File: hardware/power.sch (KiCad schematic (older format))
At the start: 16 parts, among them CON1 VEXT, P6 VEXT, U6 LD3985M33R

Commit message: LTC4417 for automatic power source switching
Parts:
- removed D1: FSV1045V, rgb-matrix:DIODE-TO-277A, symbol D_Schottky_Small
- removed D2: CDBA340L, Diodes_SMD:SMA_Standard, symbol D_Schottky_Small
- added C19, C20: 10uF, Capacitors_SMD:C_0805, symbol C
- added Q1, Q2: IRF7324PBF, SO-8, symbol IRF7324PBF
- added R31, R32: 1M, symbol R
- added R33, R36: 412k, symbol R
- added R34: 33.2k, symbol R
- added R35: 100k, symbol R
- added R37: 37.4k, symbol R
- added R38: 95.3k, symbol R
- added U8: LTC4417, symbol LTC4417
- added U9: 74x2G04, symbol 74x2G04
- D1: renamed from 3V1; Comment (none) -> 3.3V
- D2: renamed from Vext1; Comment (none) -> VEXT
- D3: renamed from Vbus1; Comment (none) -> VBUS
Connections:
- net labels added: VCC
- wire segments 36 -> 109
- no-connect marks 0 -> 4
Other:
- moved on the sheet: C12, C13, C14, C15, C9, CON1, D1, D2, D3, P6, R28, R29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

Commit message: Assign footprints
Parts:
- Q1, Q2: footprint SO-8 -> Power_Integrations:SO-8
- R31, R32, R33, R34, R35, R36, R37, R38: footprint (none) -> Resistors_SMD:R_0805
- U8: footprint (none) -> Housings_SSOP:SSOP-24_3.9x8.7mm_Pitch0.635mm
- U9: footprint (none) -> TO_SOT_Packages_SMD:SOT-23-6
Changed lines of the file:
@@
 F 0 "U8" H 4300 5000 60  0000 C CNN
 F 1 "LTC4417" H 4300 5200 60  0000 C CNN
-F 2 "" H 4300 5100 60  0001 C CNN
+F 2 "Housings_SSOP:SSOP-24_3.9x8.7mm_Pitch0.635mm" H 4300 5100 60  0001 C CNN
 F 3 "" H 4300 5100 60  0001 C CNN
 	1    4300 5100
@@
 F 0 "R31" V 6080 4000 50  0000 C CNN
 F 1 "1M" V 6000 4000 50  0000 C CNN
-F 2 "" V 5930 4000 50  0000 C CNN
+F 2 "Resistors_SMD:R_0805" V 5930 4000 50  0001 C CNN
 F 3 "" H 6000 4000 50  0000 C CNN
 	1    6000 4000
@@
 F 0 "R32" V 6230 4000 50  0000 C CNN
 F 1 "1M" V 6150 4000 50  0000 C CNN
-F 2 "" V 6080 4000 50  0000 C CNN
+F 2 "Resistors_SMD:R_0805" V 6080 4000 50  0001 C CNN
 F 3 "" H 6150 4000 50  0000 C CNN
 	1    6150 4000
@@
 F 0 "Q1" V 3350 2100 50  0000 L CNN
 F 1 "IRF7324PBF" V 3450 1700 50  0000 L CNN
-F 2 "SO-8" H 3350 2075 50  0001 L CNN
+F 2 "Power_Integrations:SO-8" H 3350 2075 50  0001 L CNN
 F 3 "" H 2400 2550 50  0000 L CNN
 	1    3100 2150
@@
 F 0 "Q1" V 3850 2100 50  0000 L CNN
 F 1 "IRF7324PBF" H 3850 2150 50  0001 L CNN
-F 2 "SO-8" H 3850 2075 50  0001 L CNN
+F 2 "Power_Integrations:SO-8" H 3850 2075 50  0001 L CNN
 F 3 "" H 2900 2550 50  0000 L CNN
 	2    3600 2150
@@
 F 0 "Q2" V 4250 2800 50  0000 L CNN
 F 1 "IRF7324PBF" V 4350 2400 50  0000 L CNN
-F 2 "SO-8" H 4250 2775 50  0001 L CNN
+F 2 "Power_Integrations:SO-8" H 4250 2775 50  0001 L CNN
 F 3 "" H 3300 3250 50  0000 L CNN
 	1    4000 2850
@@
 F 0 "Q2" V 4750 2800 50  0000 L CNN
 F 1 "IRF7324PBF" H 4750 2850 50  0001 L CNN
-F 2 "SO-8" H 4750 2775 50  0001 L CNN
+F 2 "Power_Integrations:SO-8" H 4750 2775 50  0001 L CNN
 F 3 "" H 3800 3250 50  0000 L CNN
 	2    4500 2850
@@
 F 0 "R36" V 2880 3950 50  0000 C CNN
 F 1 "412k" V 2800 3950 50  0000 C CNN
-F 2 "" V 2730 3950 50  0000 C CNN
+F 2 "Resistors_SMD:R_0805" V 2730 3950 50  0001 C CNN
 F 3 "" H 2800 3950 50  0000 C CNN
 	1    2800 3950
@@
 F 0 "R37" V 2880 4250 50  0000 C CNN
 F 1 "37.4k" V 2800 4250 50  0000 C CNN
-F 2 "" V 2730 4250 50  0000 C CNN
+F 2 "Resistors_SMD:R_0805" V 2730 4250 50  0001 C CNN
 F 3 "" H 2800 4250 50  0000 C CNN
 	1    2800 4250
@@
 F 0 "R33" V 2780 5050 50  0000 C CNN
 F 1 "412k" V 2700 5050 50  0000 C CNN
-F 2 "" V 2630 5050 50  0000 C CNN
+F 2 "Resistors_SMD:R_0805" V 2630 5050 50  0001 C CNN
 F 3 "" H 2700 5050 50  0000 C CNN
 	1    2700 5050
@@
 F 0 "R34" V 2780 5350 50  0000 C CNN
 F 1 "33.2k" V 2700 5350 50  0000 C CNN
-F 2 "" V 2630 5350 50  0000 C CNN
+F 2 "Resistors_SMD:R_0805" V 2630 5350 50  0001 C CNN
 F 3 "" H 2700 5350 50  0000 C CNN
 	1    2700 5350
@@
 F 0 "R38" V 2880 4550 50  0000 C CNN
 F 1 "95.3k" V 2800 4550 50  0000 C CNN
-F 2 "" V 2730 4550 50  0000 C CNN
+F 2 "Resistors_SMD:R_0805" V 2730 4550 50  0001 C CNN
 F 3 "" H 2800 4550 50  0000 C CNN
 	1    2800 4550
@@
 F 0 "R35" V 2780 5650 50  0000 C CNN
 F 1 "100k" V 2700 5650 50  0000 C CNN
-F 2 "" V 2630 5650 50  0000 C CNN
+F 2 "Resistors_SMD:R_0805" V 2630 5650 50  0001 C CNN
 F 3 "" H 2700 5650 50  0000 C CNN
 	1    2700 5650
@@
 F 0 "U9" H 6895 4315 50  0000 C CNN
 F 1 "74x2G04" H 6890 4075 50  0000 C CNN
-F 2 "" H 6700 4200 50  0000 C CNN
+F 2 "TO_SOT_Packages_SMD:SOT-23-6" H 6700 4200 50  0001 C CNN
 F 3 "" H 6700 4200 50  0000 C CNN
 	1    6700 4200
@@
 F 0 "U9" H 6895 4815 50  0000 C CNN
 F 1 "74x2G04" H 6890 4575 50  0000 C CNN
-F 2 "" H 6700 4700 50  0000 C CNN
+F 2 "TO_SOT_Packages_SMD:SOT-23-6" H 6700 4700 50  0001 C CNN
 F 3 "" H 6700 4700 50  0000 C CNN
 	2    6700 4700
@@
 	3450 3350 3450 2350
 Wire Wire Line
-	3150 2350 3450 2350
-Wire Wire Line
-	3450 2350 3550 2350
+	3150 2350 3550 2350
 Wire Wire Line
 	3350 2050 3350 3350
@@
 	5250 3300 5250 3350
 Wire Wire Line
-	4900 3300 5150 3300
-Wire Wire Line
-	5150 3300 5250 3300
+	4900 3300 5250 3300
 Wire Wire Line
 	5150 3350 5150 3300
@@
 	2850 6600 2900 6600
 Wire Wire Line
-	2850 6000 2850 6300
-Wire Wire Line
-	2850 6300 2850 6600
-Wire Wire Line
-	2850 6600 2850 6650
-Wire Wire Line
-	6150 4150 6150 4300
-Wire Wire Line
-	6150 4300 6150 4700
+	2850 6000 2850 6650
+Wire Wire Line
+	6150 4150 6150 4700
 Wire Wire Line
 	5700 4300 6150 4300
@@
 	6000 4200 6000 4150
 Wire Wire Line
-	5700 4200 6000 4200
-Wire Wire Line
-	6000 4200 6250 4200
-Wire Wire Line
-	6000 3750 6000 3800
-Wire Wire Line
-	6000 3800 6000 3850
+	5700 4200 6250 4200
+Wire Wire Line
+	6000 3750 6000 3850
 Wire Wire Line
 	6150 3800 6000 3800
@@
 	5700 6350 5800 6350
 Wire Wire Line
-	1200 2650 2150 2650
-Wire Wire Line
-	2150 2650 2700 2650
-Wire Wire Line
-	2700 2650 3800 2650
+	1200 2650 3800 2650
 Wire Wire Line
 	9550 1500 9550 1600
@@
 	1550 1400 1200 1400
 Wire Wire Line
-	1550 1950 1650 1950
-Wire Wire Line
-	1650 1950 2150 1950
-Wire Wire Line
-	2150 1950 2800 1950
-Wire Wire Line
-	2800 1950 2900 1950
+	1550 1950 2900 1950
 Connection ~ 1550 2150
 Wire Wire Line
-	1550 2050 1550 2150
-Wire Wire Line
-	1550 2150 1550 2250
+	1550 2050 1550 2250
 Connection ~ 8700 1600
 Wire Wire Line
@@
 Connection ~ 7050 2150
 Wire Wire Line
-	7050 2150 7250 2150
-Wire Wire Line
-	7250 2150 7800 2150
-Wire Wire Line
-	7800 2150 8250 2150
-Wire Wire Line
-	8250 2150 8450 2150
-Wire Wire Line
-	8450 2150 8700 2150
+	7050 2150 8700 2150
 Connection ~ 7250 1750
 Connection ~ 7050 1600
 Connection ~ 7250 1600
 Wire Wire Line
-	7250 1600 7250 1750
-Wire Wire Line
-	7250 1750 7250 1850
+	7250 1600 7250 1850
 Wire Wire Line
 	7350 1750 7250 1750
 Wire Wire Line
-	8250 1600 8450 1600
-Wire Wire Line
-	8450 1600 8700 1600
-Wire Wire Line
-	7050 1600 7250 1600
-Wire Wire Line
-	7250 1600 7350 1600
-Wire Wire Line
-	7050 1550 7050 1600
-Wire Wire Line
-	7050 1600 7050 1700
-Wire Wire Line
-	8700 1450 8700 1600
-Wire Wire Line
-	8700 1600 8700 1850
+	8250 1600 8700 1600
+Wire Wire Line
+	7050 1600 7350 1600
+Wire Wire Line
+	7050 1550 7050 1700
+Wire Wire Line
+	8700 1450 8700 1850
 Wire Wire Line
 	8450 2150 8450 1950
 Wire Wire Line
-	7050 2000 7050 2150
-Wire Wire Line
-	7050 2150 7050 2200
+	7050 2000 7050 2200
 Wire Wire Line
 	3800 2650 3800 2750
@@
 	4450 3100 4450 3050
 Wire Wire Line
-	4050 3100 4350 3100
-Wire Wire Line
-	4350 3100 4450 3100
+	4050 3100 4450 3100
 Wire Wire Line
 	4050 3050 4050 3100
 Connection ~ 4250 2750
 Wire Wire Line
-	4200 2750 4250 2750
-Wire Wire Line
-	4250 2750 4300 2750
+	4200 2750 4300 2750
 Wire Wire Line
 	4250 2750 4250 3350
@@
 Connection ~ 3350 2050
 Wire Wire Line
-	3300 2050 3350 2050
-Wire Wire Line
-	3350 2050 3400 2050
+	3300 2050 3400 2050
 Connection ~ 5150 3300
 Wire Wire Line
-	5750 1850 5750 1950
-Wire Wire Line
-	5750 1950 5750 2650
-Wire Wire Line
-	5750 2650 5750 3800
+	5750 1850 5750 3800
 Wire Wire Line
 	4700 2650 4700 2750
@@
 Connection ~ 5750 2650
 Wire Wire Line
-	10850 1450 10850 1700
+	10850 1700 10850 1450
 Wire Wire Line
 	10600 1450 10600 1700
@@
 	10350 1450 10350 1700
 Wire Wire Line
-	10350 1700 10600 1700
-Wire Wire Line
-	10600 1700 10850 1700
+	10350 1700 10850 1700
 Connection ~ 10600 1700
 $EndSCHEMATC

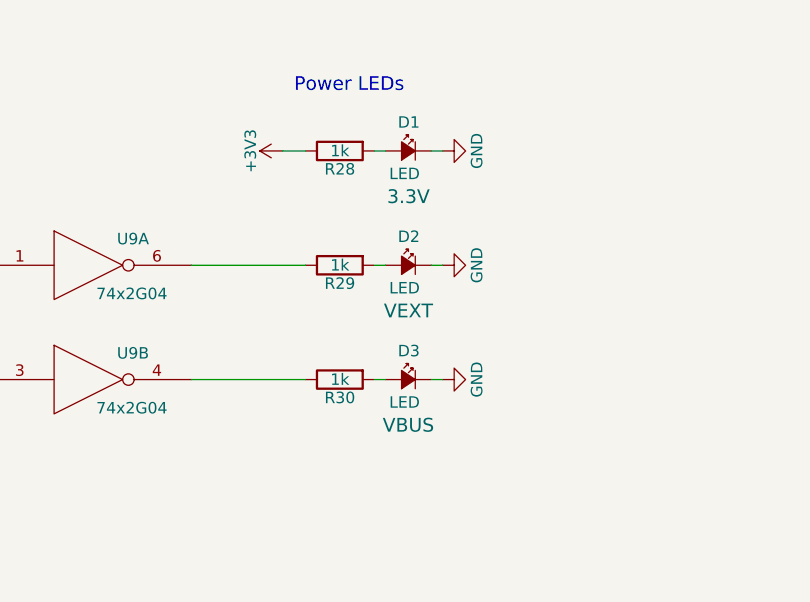
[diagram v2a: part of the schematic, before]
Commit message: Fix IRF7324 footprint
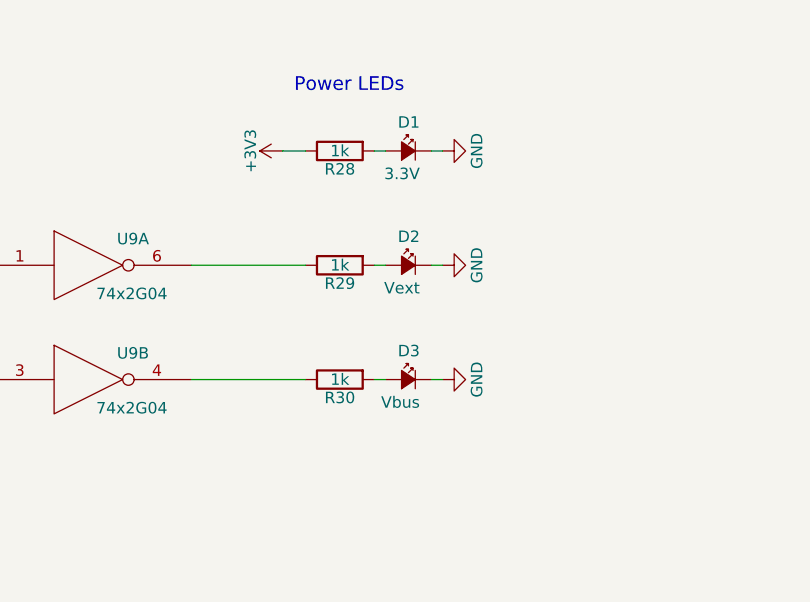
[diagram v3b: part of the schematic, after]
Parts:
- D1: value LED -> 3.3V; Comment 3.3V -> (none)
- D2: value LED -> Vext; Comment VEXT -> (none)
- D3: value LED -> Vbus; Comment VBUS -> (none)
- Q1, Q2: footprint Power_Integrations:SO-8 -> rgb-matrix:SOIC-8
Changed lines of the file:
@@
 P 8100 4200
 F 0 "D2" H 8050 4325 50  0000 L CNN
-F 1 "LED" H 8050 4100 50  0000 L CNN
+F 1 "Vext" H 8050 4100 50  0000 L CNN
 F 2 "LEDs:LED_1206" V 8100 4200 50  0001 C CNN
 F 3 "" V 8100 4200 50  0000 C CNN
-F 4 "VEXT" H 8100 4000 60  0000 C CNN "Comment"
 	1    8100 4200
 	-1   0    0    -1
@@
 P 8100 4700
 F 0 "D3" H 8050 4825 50  0000 L CNN
-F 1 "LED" H 8050 4600 50  0000 L CNN
+F 1 "Vbus" H 8050 4600 50  0000 L CNN
 F 2 "LEDs:LED_1206" V 8100 4700 50  0001 C CNN
 F 3 "" V 8100 4700 50  0000 C CNN
-F 4 "VBUS" H 8100 4500 60  0000 C CNN "Comment"
 	1    8100 4700
 	-1   0    0    -1
@@
 P 8100 3700
 F 0 "D1" H 8050 3825 50  0000 L CNN
-F 1 "LED" H 8050 3600 50  0000 L CNN
+F 1 "3.3V" H 8050 3600 50  0000 L CNN
 F 2 "LEDs:LED_1206" V 8100 3700 50  0001 C CNN
 F 3 "" V 8100 3700 50  0000 C CNN
-F 4 "3.3V" H 8100 3500 60  0000 C CNN "Comment"
 	1    8100 3700
 	-1   0    0    -1
@@
 F 0 "Q1" V 3350 2100 50  0000 L CNN
 F 1 "IRF7324PBF" V 3450 1700 50  0000 L CNN
-F 2 "Power_Integrations:SO-8" H 3350 2075 50  0001 L CNN
+F 2 "rgb-matrix:SOIC-8" H 3350 2075 50  0001 L CNN
 F 3 "" H 2400 2550 50  0000 L CNN
 	1    3100 2150
@@
 F 0 "Q1" V 3850 2100 50  0000 L CNN
 F 1 "IRF7324PBF" H 3850 2150 50  0001 L CNN
-F 2 "Power_Integrations:SO-8" H 3850 2075 50  0001 L CNN
+F 2 "rgb-matrix:SOIC-8" H 3850 2075 50  0001 L CNN
 F 3 "" H 2900 2550 50  0000 L CNN
 	2    3600 2150
@@
 F 0 "Q2" V 4250 2800 50  0000 L CNN
 F 1 "IRF7324PBF" V 4350 2400 50  0000 L CNN
-F 2 "Power_Integrations:SO-8" H 4250 2775 50  0001 L CNN
+F 2 "rgb-matrix:SOIC-8" H 4250 2775 50  0001 L CNN
 F 3 "" H 3300 3250 50  0000 L CNN
 	1    4000 2850
@@
 F 0 "Q2" V 4750 2800 50  0000 L CNN
 F 1 "IRF7324PBF" H 4750 2850 50  0001 L CNN
-F 2 "Power_Integrations:SO-8" H 4750 2775 50  0001 L CNN
+F 2 "rgb-matrix:SOIC-8" H 4750 2775 50  0001 L CNN
 F 3 "" H 3800 3250 50  0000 L CNN
 	2    4500 2850

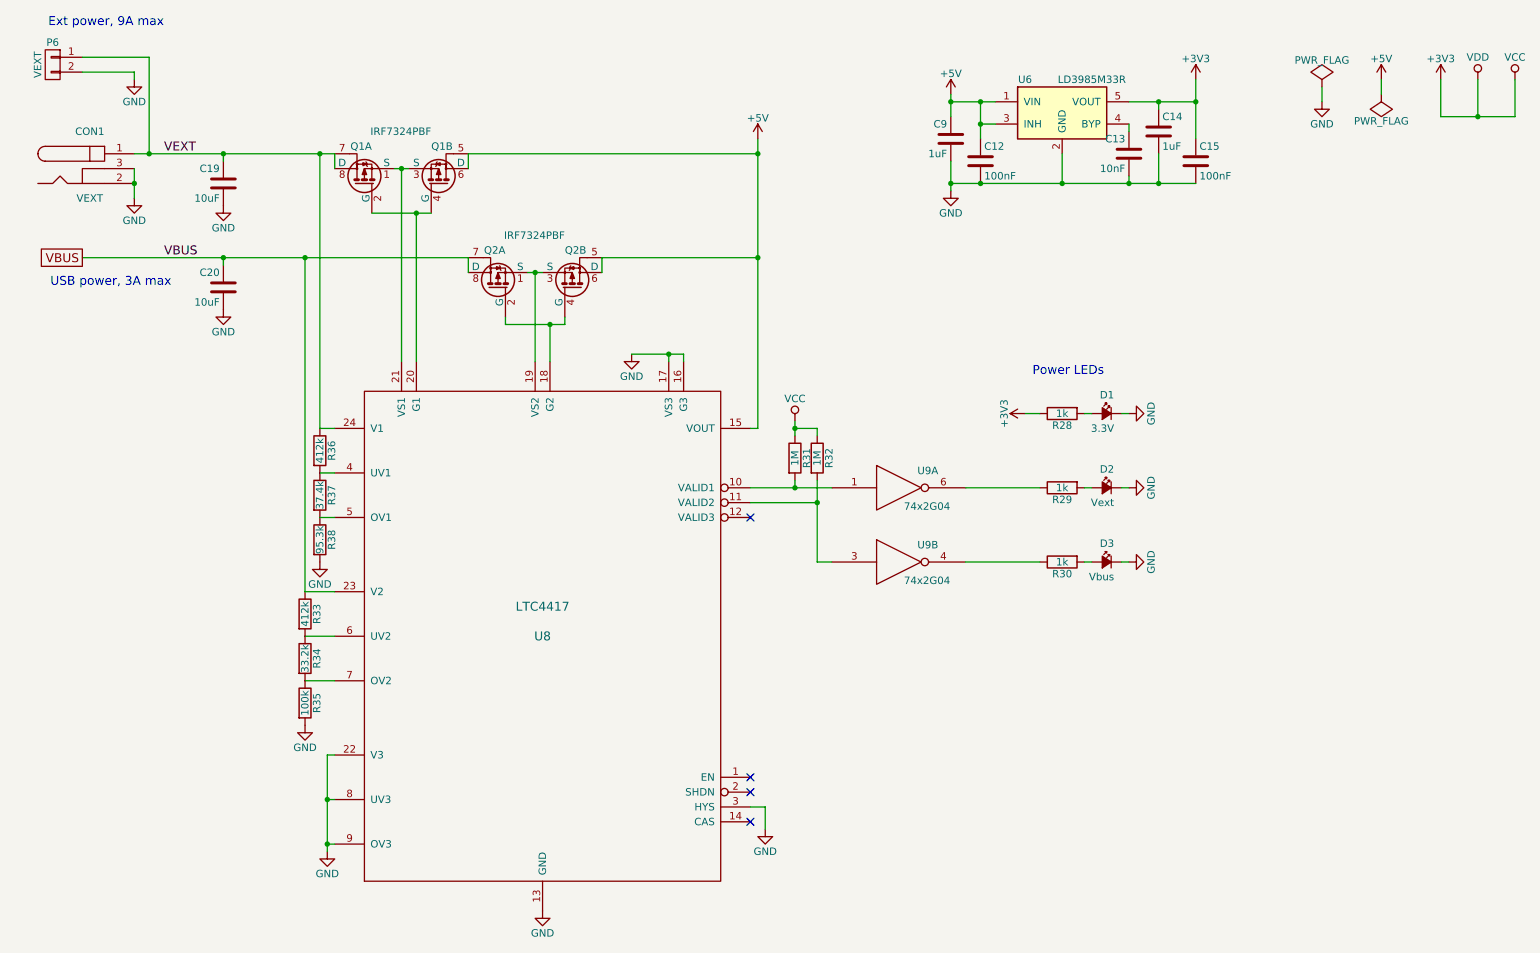
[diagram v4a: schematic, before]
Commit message: Remove LTC4417, replace with solder bridges
Simply not enough space on the board!
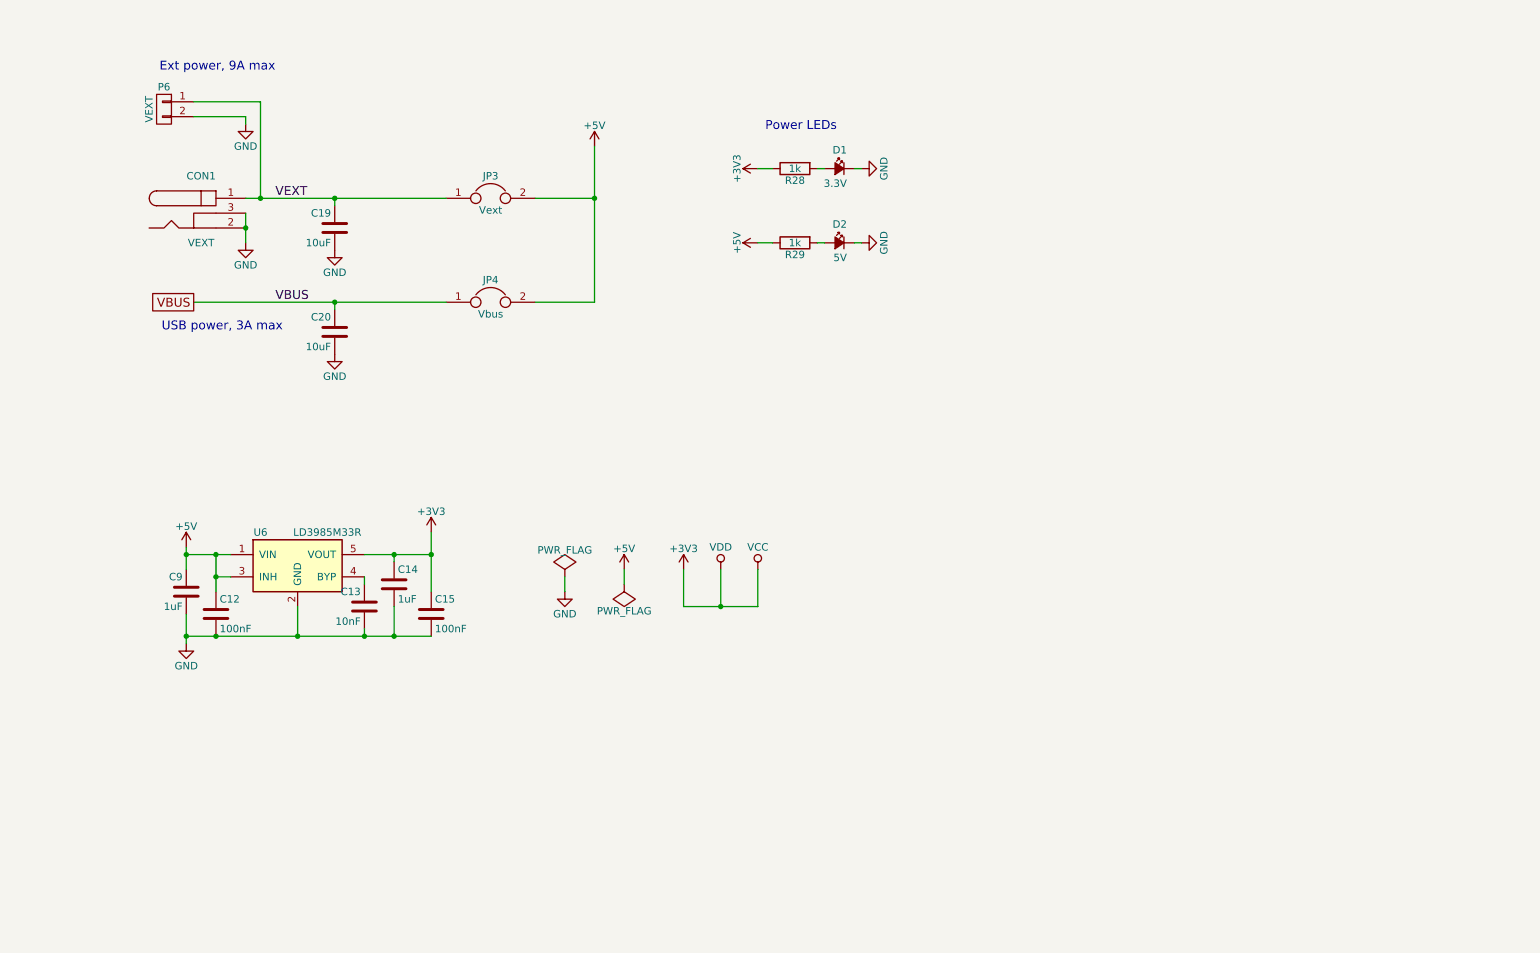
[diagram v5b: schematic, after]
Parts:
- removed D3: Vbus, LEDs:LED_1206, symbol Led_Small
- removed Q1, Q2: IRF7324PBF, rgb-matrix:SOIC-8, symbol IRF7324PBF
- removed R30: 1k, Resistors_SMD:R_0805, symbol R
- removed R31, R32: 1M, Resistors_SMD:R_0805, symbol R
- removed R33, R36: 412k, Resistors_SMD:R_0805, symbol R
- removed R34: 33.2k, Resistors_SMD:R_0805, symbol R
- removed R35: 100k, Resistors_SMD:R_0805, symbol R
- removed R37: 37.4k, Resistors_SMD:R_0805, symbol R
- removed R38: 95.3k, Resistors_SMD:R_0805, symbol R
- removed U8: LTC4417, Housings_SSOP:SSOP-24_3.9x8.7mm_Pitch0.635mm, symbol LTC4417
- removed U9: 74x2G04, TO_SOT_Packages_SMD:SOT-23-6, symbol 74x2G04
- added JP3: Vext, rgb-matrix:SMD-solder-bridge-3mm, symbol Jumper
- added JP4: Vbus, rgb-matrix:SMD-solder-bridge-3mm, symbol Jumper
- D2: value Vext -> 5V
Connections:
- net +5V: now also R29.1, JP3.2, JP4.2
- net VBUS: now also JP4.1
- net VEXT: now also JP3.1
- no-connect marks 4 -> 0
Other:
- moved on the sheet: C12, C13, C14, C15, C19, C20, C9, CON1, D1, D2, P6, R28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
